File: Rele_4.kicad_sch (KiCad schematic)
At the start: 6 parts, among them J12 Rele_4, J30 Pin GND, K1 SRD-05VDC-SL-C, Q9 PMBT3904,235

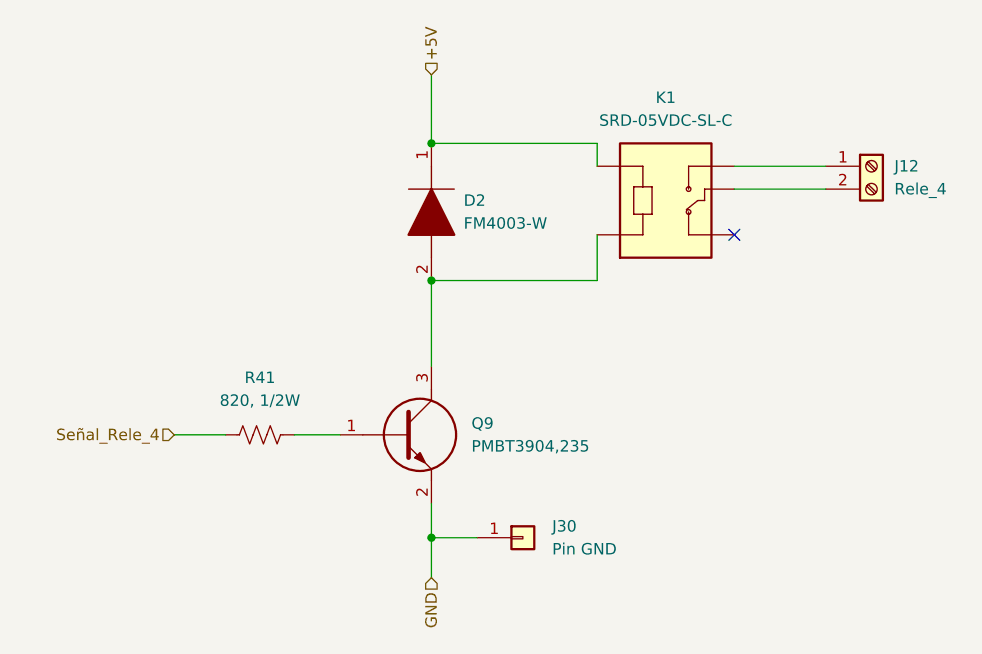
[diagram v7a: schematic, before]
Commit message: Se modificaron algunos componentes, según disponibilidad
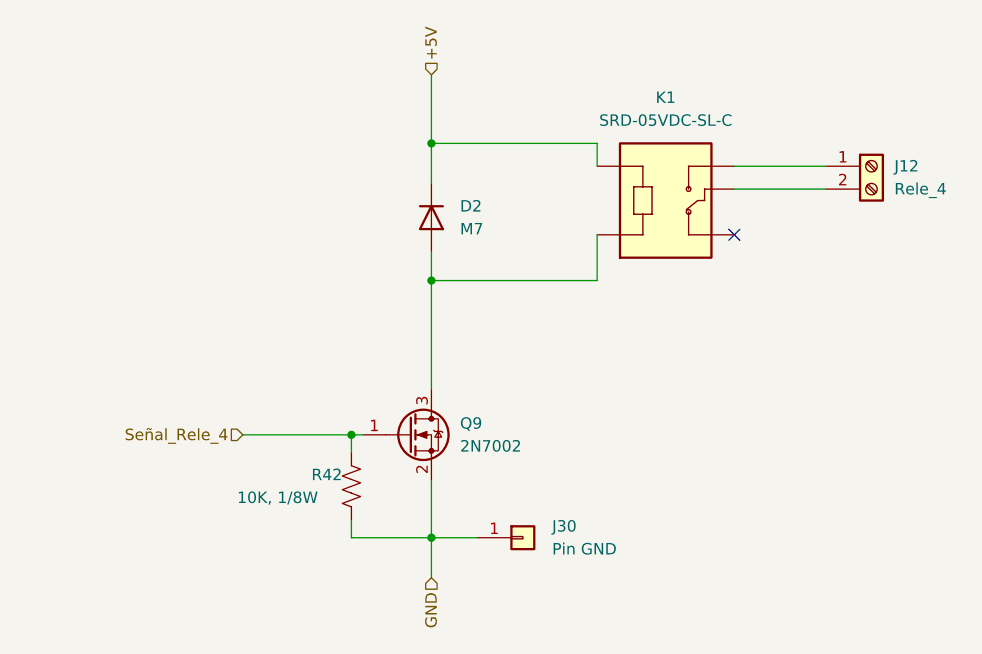
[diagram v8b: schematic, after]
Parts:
- removed D2: FM4003-W, FM4003W:DIOM5025X231N, symbol FM4003-W:FM4003-W
- removed Q9: PMBT3904,235, PMBT3904,235:SOT95P230X110-3N, symbol PMBT3904,235:PMBT3904,235
- removed R41: 820, 1/2W, Resistor_SMD:R_0805_2012Metric, symbol Device:R_US
- added D2: M7, Diode_SMD:D_SMA, symbol Device:D
- added Q9: 2N7002, Package_TO_SOT_SMD:SOT-23, symbol Transistor_FET:2N7002
- added R42: 10K, 1/8W, Resistor_SMD:R_0805_2012Metric, symbol Device:R_US
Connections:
- net +5V: now also D2.1 (K)
- net GND: now also Q9.2 (S), R42.2
- net Señal_Rele_4: now also Q9.1 (G), R42.1
- net at K1.A2: now also D2.2 (A), Q9.3 (D)
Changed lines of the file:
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@@
   (junction (at 142.875 116.205) (diameter 0) (color 0 0 0 0)
+  )
+  (junction (at 133.985 104.775) (diameter 0) (color 0 0 0 0)
   )
   (junction (at 142.875 87.63) (diameter 0) (color 0 0 0 0)
@@
     (stroke (width 0) (type default) (color 0 0 0 0))
   )
-  (wire (pts (xy 142.875 87.63) (xy 142.875 97.155))
+  (wire (pts (xy 142.875 87.63) (xy 142.875 99.695))
     (stroke (width 0) (type default) (color 0 0 0 0))
   )
-  (wire (pts (xy 142.875 112.395) (xy 142.875 116.205))
+  (wire (pts (xy 142.875 109.855) (xy 142.875 116.205))
+    (stroke (width 0) (type default) (color 0 0 0 0))
+  )
+  (wire (pts (xy 133.985 104.775) (xy 133.985 106.68))
     (stroke (width 0) (type default) (color 0 0 0 0))
   )
   (wire (pts (xy 161.29 87.63) (xy 161.29 82.55))
+    (stroke (width 0) (type default) (color 0 0 0 0))
+  )
+  (wire (pts (xy 142.875 72.39) (xy 142.875 76.835))
     (stroke (width 0) (type default) (color 0 0 0 0))
   )
@@
     (stroke (width 0) (type default) (color 0 0 0 0))
   )
-  (wire (pts (xy 114.3 104.775) (xy 120.015 104.775))
+  (wire (pts (xy 133.985 114.3) (xy 133.985 116.205))
+    (stroke (width 0) (type default) (color 0 0 0 0))
+  )
+  (wire (pts (xy 133.985 116.205) (xy 142.875 116.205))
+    (stroke (width 0) (type default) (color 0 0 0 0))
+  )
+  (wire (pts (xy 133.985 104.775) (xy 135.255 104.775))
     (stroke (width 0) (type default) (color 0 0 0 0))
   )
@@
     (stroke (width 0) (type default) (color 0 0 0 0))
   )
-  (wire (pts (xy 127.635 104.775) (xy 132.715 104.775))
+  (wire (pts (xy 121.92 104.775) (xy 133.985 104.775))
+    (stroke (width 0) (type default) (color 0 0 0 0))
+  )
+  (wire (pts (xy 142.875 84.455) (xy 142.875 87.63))
     (stroke (width 0) (type default) (color 0 0 0 0))
   )
@@
     (effects (font (size 1.27 1.27)) (justify left))
   )
-  (hierarchical_label "Señal_Rele_4" (shape input) (at 114.3 104.775 180)
+  (hierarchical_label "Señal_Rele_4" (shape input) (at 121.92 104.775 180)
     (effects (font (size 1.27 1.27)) (justify right))
   )
   (hierarchical_label "GND" (shape input) (at 142.875 120.65 270)
     (effects (font (size 1.27 1.27)) (justify right))
+  )
+  (symbol (lib_id "Device:R_US") (at 133.985 110.49 0) (unit 1)
+    (in_bom yes) (on_board yes)
+    (property "Reference" "R42" (id 0) (at 129.54 109.22 0)
+      (effects (font (size 1.27 1.27)) (justify left))
+    )
+    (property "Value" "10K, 1/8W" (id 1) (at 121.285 111.76 0)
+      (effects (font (size 1.27 1.27)) (justify left))
+    )
+    (property "Footprint" "Resistor_SMD:R_0805_2012Metric" (id 2) (at 135.001 110.744 90)
+      (effects (font (size 1.27 1.27)) hide)
+    )
+    (property "Datasheet" "~" (id 3) (at 133.985 110.49 0)
+      (effects (font (size 1.27 1.27)) hide)
+    )
+    (pin "1")
+    (pin "2")
   )
   (symbol (lib_id "Connector_Generic:Conn_01x01") (at 153.035 116.205 0) (unit 1)
@@
     (pin "1")
   )
-  (symbol (lib_id "Device:R_US") (at 123.825 104.775 90) (unit 1)
+  (symbol (lib_id "Device:D") (at 142.875 80.645 270) (unit 1)
     (in_bom yes) (on_board yes) (fields_autoplaced)
-    (property "Reference" "R41" (id 0) (at 123.825 98.425 90))
-    (property "Value" "820, 1/2W" (id 1) (at 123.825 100.965 90))
-    (property "Footprint" "Resistor_SMD:R_0805_2012Metric" (id 2) (at 124.079 103.759 90)
+    (property "Reference" "D2" (id 0) (at 146.05 79.3749 90)
+      (effects (font (size 1.27 1.27)) (justify left))
+    )
+    (property "Value" "M7" (id 1) (at 146.05 81.9149 90)
+      (effects (font (size 1.27 1.27)) (justify left))
+    )
+    (property "Footprint" "Diode_SMD:D_SMA" (id 2) (at 142.875 80.645 0)
       (effects (font (size 1.27 1.27)) hide)
     )
-    (property "Datasheet" "~" (id 3) (at 123.825 104.775 0)
+    (property "Datasheet" "~" (id 3) (at 142.875 80.645 0)
       (effects (font (size 1.27 1.27)) hide)
     )
@@
     (pin "2")
   )
-  (symbol (lib_id "PMBT3904,235:PMBT3904,235") (at 132.715 104.775 0) (unit 1)
+  (symbol (lib_id "Transistor_FET:2N7002") (at 140.335 104.775 0) (unit 1)
     (in_bom yes) (on_board yes) (fields_autoplaced)
-    (property "Reference" "Q9" (id 0) (at 147.32 103.5049 0)
+    (property "Reference" "Q9" (id 0) (at 146.05 103.5049 0)
       (effects (font (size 1.27 1.27)) (justify left))
     )
-    (property "Value" "PMBT3904,235" (id 1) (at 147.32 106.0449 0)
+    (property "Value" "2N7002" (id 1) (at 146.05 106.0449 0)
       (effects (font (size 1.27 1.27)) (justify left))
     )
-    (property "Footprint" "PMBT3904,235:SOT95P230X110-3N" (id 2) (at 146.685 108.585 0)
-      (effects (font (size 1.27 1.27)) (justify left) hide)
+    (property "Footprint" "Package_TO_SOT_SMD:SOT-23" (id 2) (at 145.415 106.68 0)
+      (effects (font (size 1.27 1.27) italic) (justify left) hide)
     )
-    (property "Datasheet" "https://assets.nexperia.com/documents/data-sheet/PMBT3904.pdf" (id 3) (at 146.685 111.125 0)
-      (effects (font (size 1.27 1.27)) (justify left) hide)
-    )
-    (property "Description" "PMBT3904 - NPN switching transistor" (id 4) (at 146.685 113.665 0)
-      (effects (font (size 1.27 1.27)) (justify left) hide)
-    )
-    (property "Height" "1.1" (id 5) (at 146.685 116.205 0)
-      (effects (font (size 1.27 1.27)) (justify left) hide)
-    )
-    (property "Manufacturer_Name" "Nexperia" (id 6) (at 146.685 118.745 0)
-      (effects (font (size 1.27 1.27)) (justify left) hide)
-    )
-    (property "Manufacturer_Part_Number" "PMBT3904,235" (id 7) (at 146.685 121.285 0)
-      (effects (font (size 1.27 1.27)) (justify left) hide)
-    )
-    (property "Mouser Part Number" "771-PMBT3904235" (id 8) (at 146.685 123.825 0)
-      (effects (font (size 1.27 1.27)) (justify left) hide)
-    )
-    (property "Mouser Price/Stock" "https://www.mouser.co.uk/ProductDetail/Nexperia/PMBT3904235?qs=LOCUfHb8d9uziIfl4fmvZg%3D%3D" (id 9) (at 146.685 126.365 0)
-      (effects (font (size 1.27 1.27)) (justify left) hide)
-    )
-    (property "Arrow Part Number" "PMBT3904,235" (id 10) (at 146.685 128.905 0)
-      (effects (font (size 1.27 1.27)) (justify left) hide)
-    )
-    (property "Arrow Price/Stock" "https://www.arrow.com/en/products/pmbt3904235/nexperia?region=nac" (id 11) (at 146.685 131.445 0)
-      (effects (font (size 1.27 1.27)) (justify left) hide)
-    )
-    (property "Mouser Testing Part Number" "" (id 12) (at 146.685 133.985 0)
-      (effects (font (size 1.27 1.27)) (justify left) hide)
-    )
-    (property "Mouser Testing Price/Stock" "" (id 13) (at 146.685 136.525 0)
+    (property "Datasheet" "https://www.onsemi.com/pub/Collateral/NDS7002A-D.PDF" (id 3) (at 140.335 104.775 0)
       (effects (font (size 1.27 1.27)) (justify left) hide)
     )
@@
     (pin "NO")
   )
-  (symbol (lib_id "FM4003-W:FM4003-W") (at 142.875 72.39 270) (unit 1)
-    (in_bom yes) (on_board yes) (fields_autoplaced)
-    (property "Reference" "D2" (id 0) (at 146.4564 78.7399 90)
-      (effects (font (size 1.27 1.27)) (justify left))
-    )
-    (property "Value" "FM4003-W" (id 1) (at 146.4564 81.2799 90)
-      (effects (font (size 1.27 1.27)) (justify left))
-    )
-    (property "Footprint" "FM4003W:DIOM5025X231N" (id 2) (at 142.875 83.82 0)
-      (effects (font (size 1.27 1.27)) (justify left) hide)
-    )
-    (property "Datasheet" "https://componentsearchengine.com/Datasheets/1/FM4003-W.pdf" (id 3) (at 140.335 83.82 0)
-      (effects (font (size 1.27 1.27)) (justify left) hide)
-    )
-    (property "Description" "Rectifiers 1A 200V GP" (id 4) (at 137.795 83.82 0)
-      (effects (font (size 1.27 1.27)) (justify left) hide)
-    )
-    (property "Height" "2.31" (id 5) (at 135.255 83.82 0)
-      (effects (font (size 1.27 1.27)) (justify left) hide)
-    )
-    (property "Manufacturer_Name" "Rectron" (id 6) (at 132.715 83.82 0)
-      (effects (font (size 1.27 1.27)) (justify left) hide)
-    )
-    (property "Manufacturer_Part_Number" "FM4003-W" (id 7) (at 130.175 83.82 0)
-      (effects (font (size 1.27 1.27)) (justify left) hide)
-    )
-    (property "Mouser Part Number" "583-FM4003-W" (id 8) (at 127.635 83.82 0)
-      (effects (font (size 1.27 1.27)) (justify left) hide)
-    )
-    (property "Mouser Price/Stock" "https://www.mouser.co.uk/ProductDetail/Rectron/FM4003-W/?qs=5h8Q3Z7TNRlJu6QU92Ho0w%3D%3D" (id 9) (at 125.095 83.82 0)
-      (effects (font (size 1.27 1.27)) (justify left) hide)
-    )
-    (property "Arrow Part Number" "FM4003-W" (id 10) (at 122.555 83.82 0)
-      (effects (font (size 1.27 1.27)) (justify left) hide)
-    )
-    (property "Arrow Price/Stock" "https://www.arrow.com/en/products/fm4003-w/rectron" (id 11) (at 120.015 83.82 0)
-      (effects (font (size 1.27 1.27)) (justify left) hide)
-    )
-    (property "Mouser Testing Part Number" "" (id 12) (at 117.475 83.82 0)
-      (effects (font (size 1.27 1.27)) (justify left) hide)
-    )
-    (property "Mouser Testing Price/Stock" "" (id 13) (at 114.935 83.82 0)
-      (effects (font (size 1.27 1.27)) (justify left) hide)
-    )
-    (pin "1")
-    (pin "2")
-  )
 )
